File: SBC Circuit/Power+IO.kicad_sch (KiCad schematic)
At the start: 41 parts, among them J1 USB_B, J2 Conn_01x02_Pin, J4 Conn_01x06_Pin, J8 Conn_01x02_Pin, J9 Conn_02x04_Odd_Even, Q1 AOI21357, Q2 AOI21357, U10 FT230XS, U8 LM7805_TO220, U9 LD1117AV33

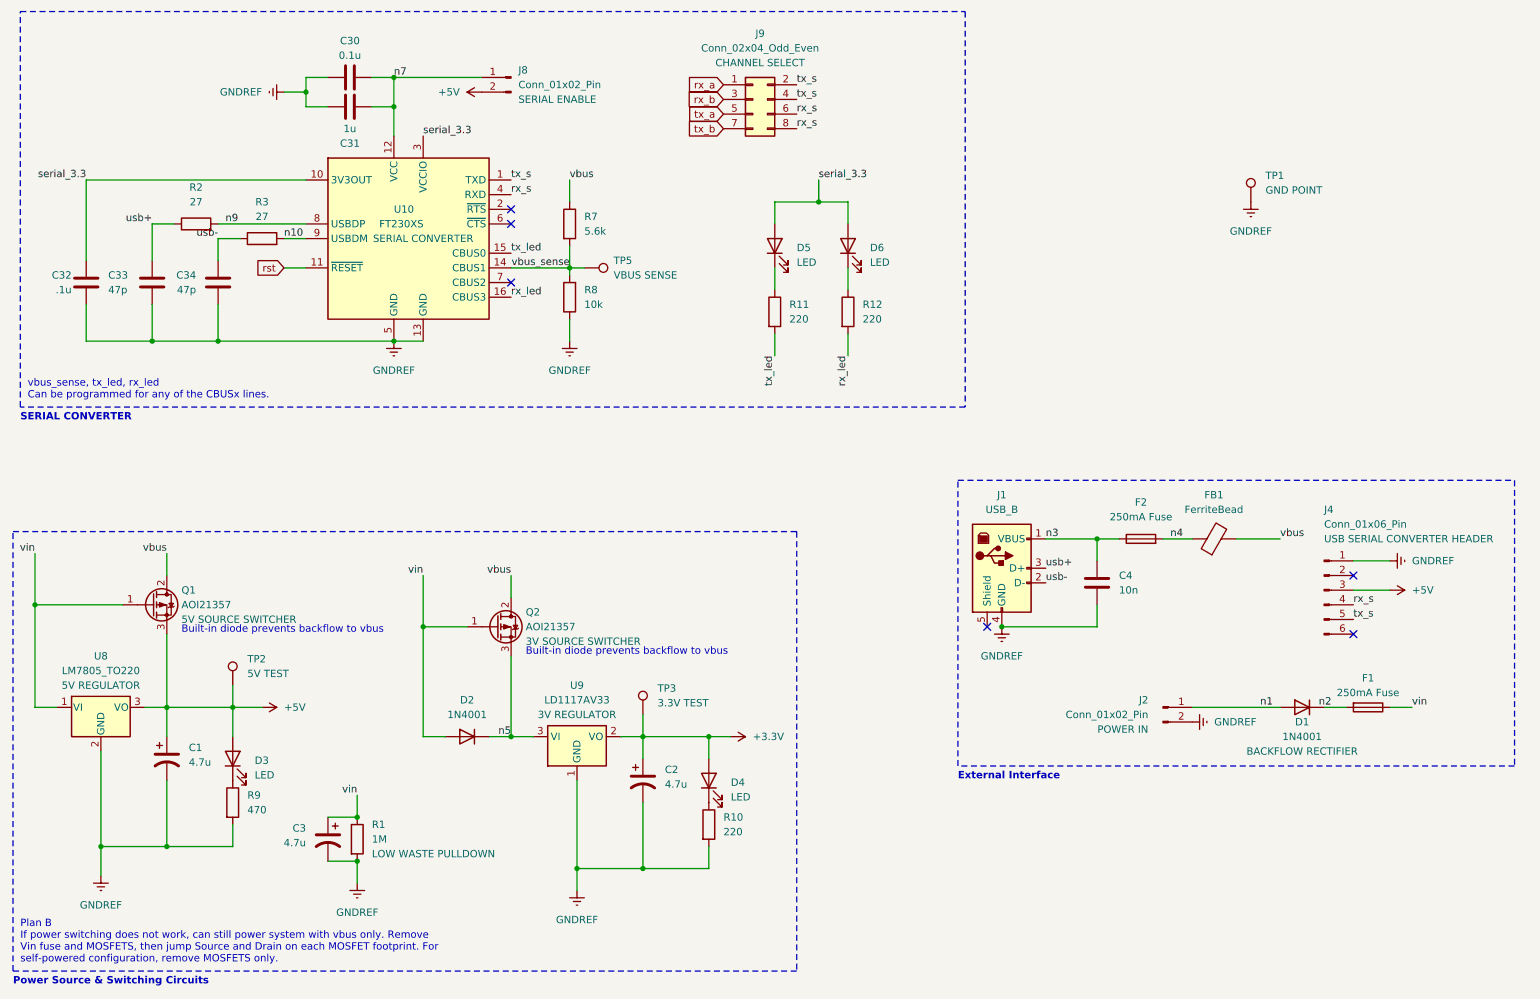
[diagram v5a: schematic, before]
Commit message: Finalize PCB, neaten up Schematic
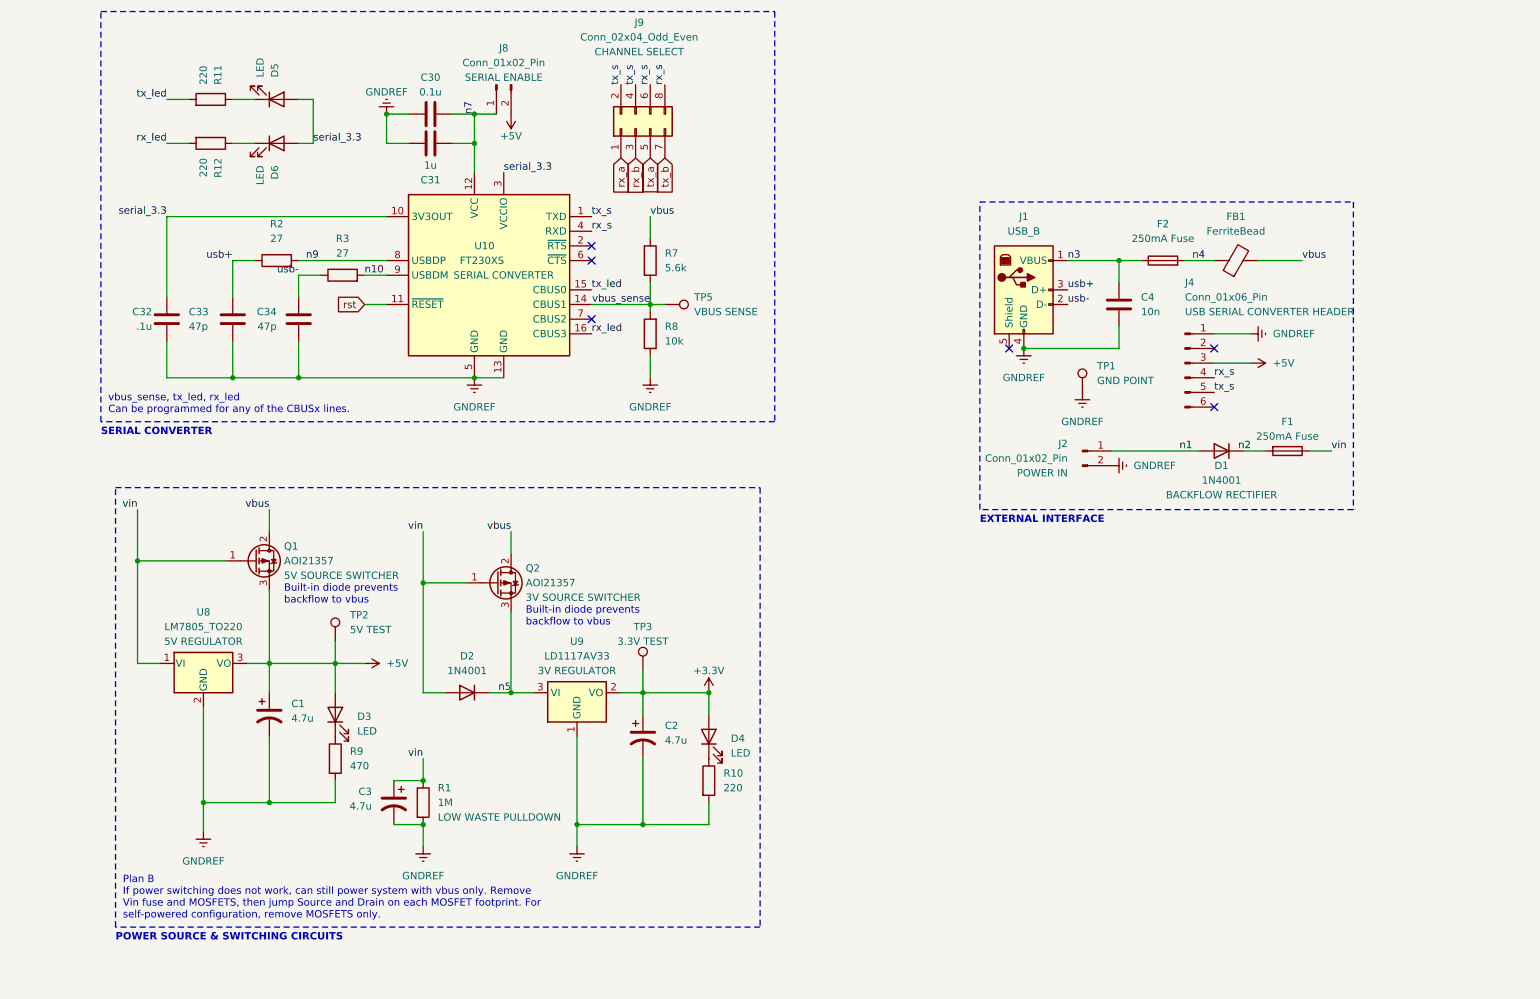
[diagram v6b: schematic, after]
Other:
- note added: "EXTERNAL INTERFACE"
- note added: "POWER SOURCE & SWITCHING CIRCUITS"
- note removed: "External Interface"
- note removed: "Power Source & Switching Circuits"
- moved on the sheet: C1, C2, C3, C30, C31, C32, C33, C34, C4, D1, D2, D3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
